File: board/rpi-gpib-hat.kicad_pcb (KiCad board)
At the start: 2 copper layers, 65 x 30 mm, 73 parts, among them J1 RPI_GPIO, J2 GPIB, U1 SN75162BDW, U2 SN75160BDW, U3 CAT24C32

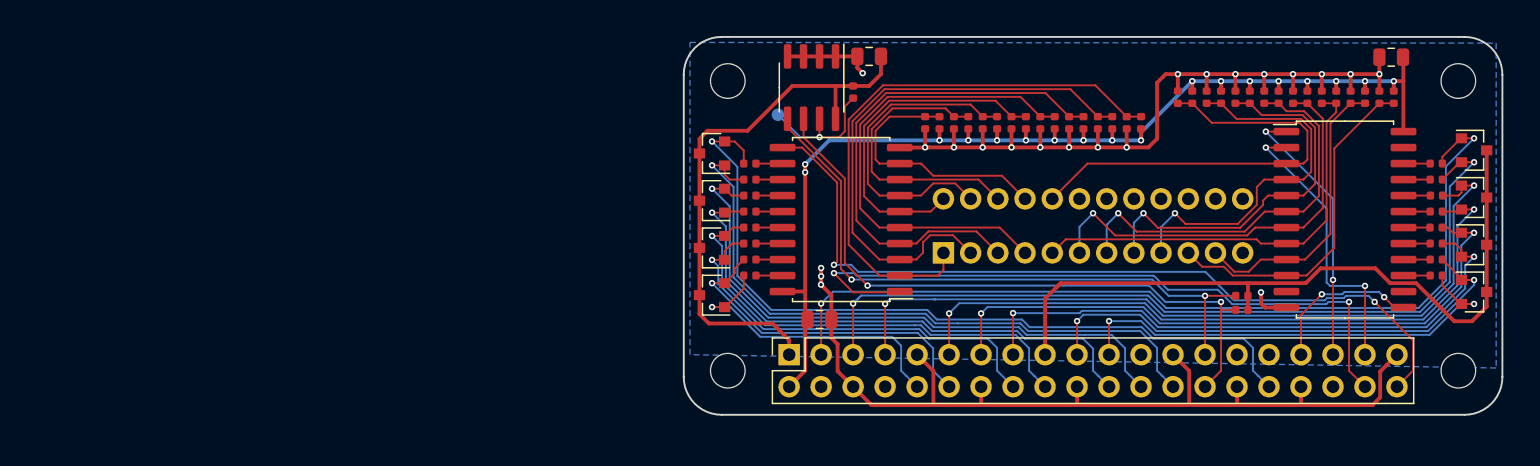
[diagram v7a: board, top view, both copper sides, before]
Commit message: Add reference designators.
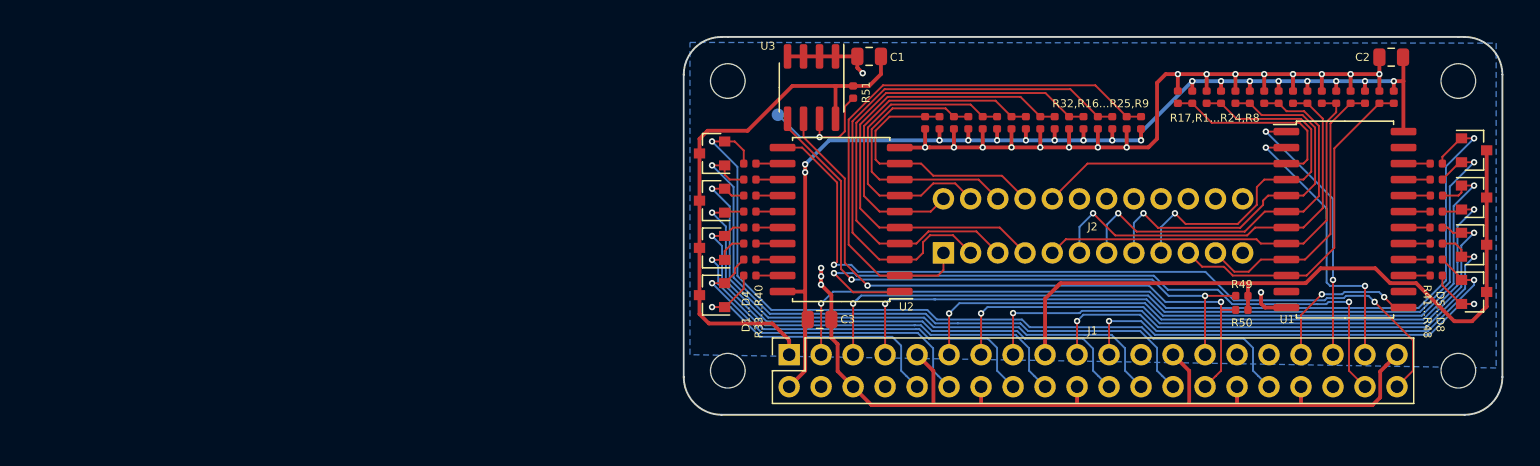
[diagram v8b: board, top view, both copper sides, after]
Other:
- board text added: "D1...D4 R33...R40"
- board text added: "D5...D8 R41...R48"
- board text added: "R17,R1...R24,R8"
- board text added: "R32,R16...R25,R9"
